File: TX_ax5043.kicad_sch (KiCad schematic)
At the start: 27 parts, among them P6 CONUFL001-SMD-T, P7 CONUFL001-SMD-T, Q7 DMP2037U-7, U23 AX5043

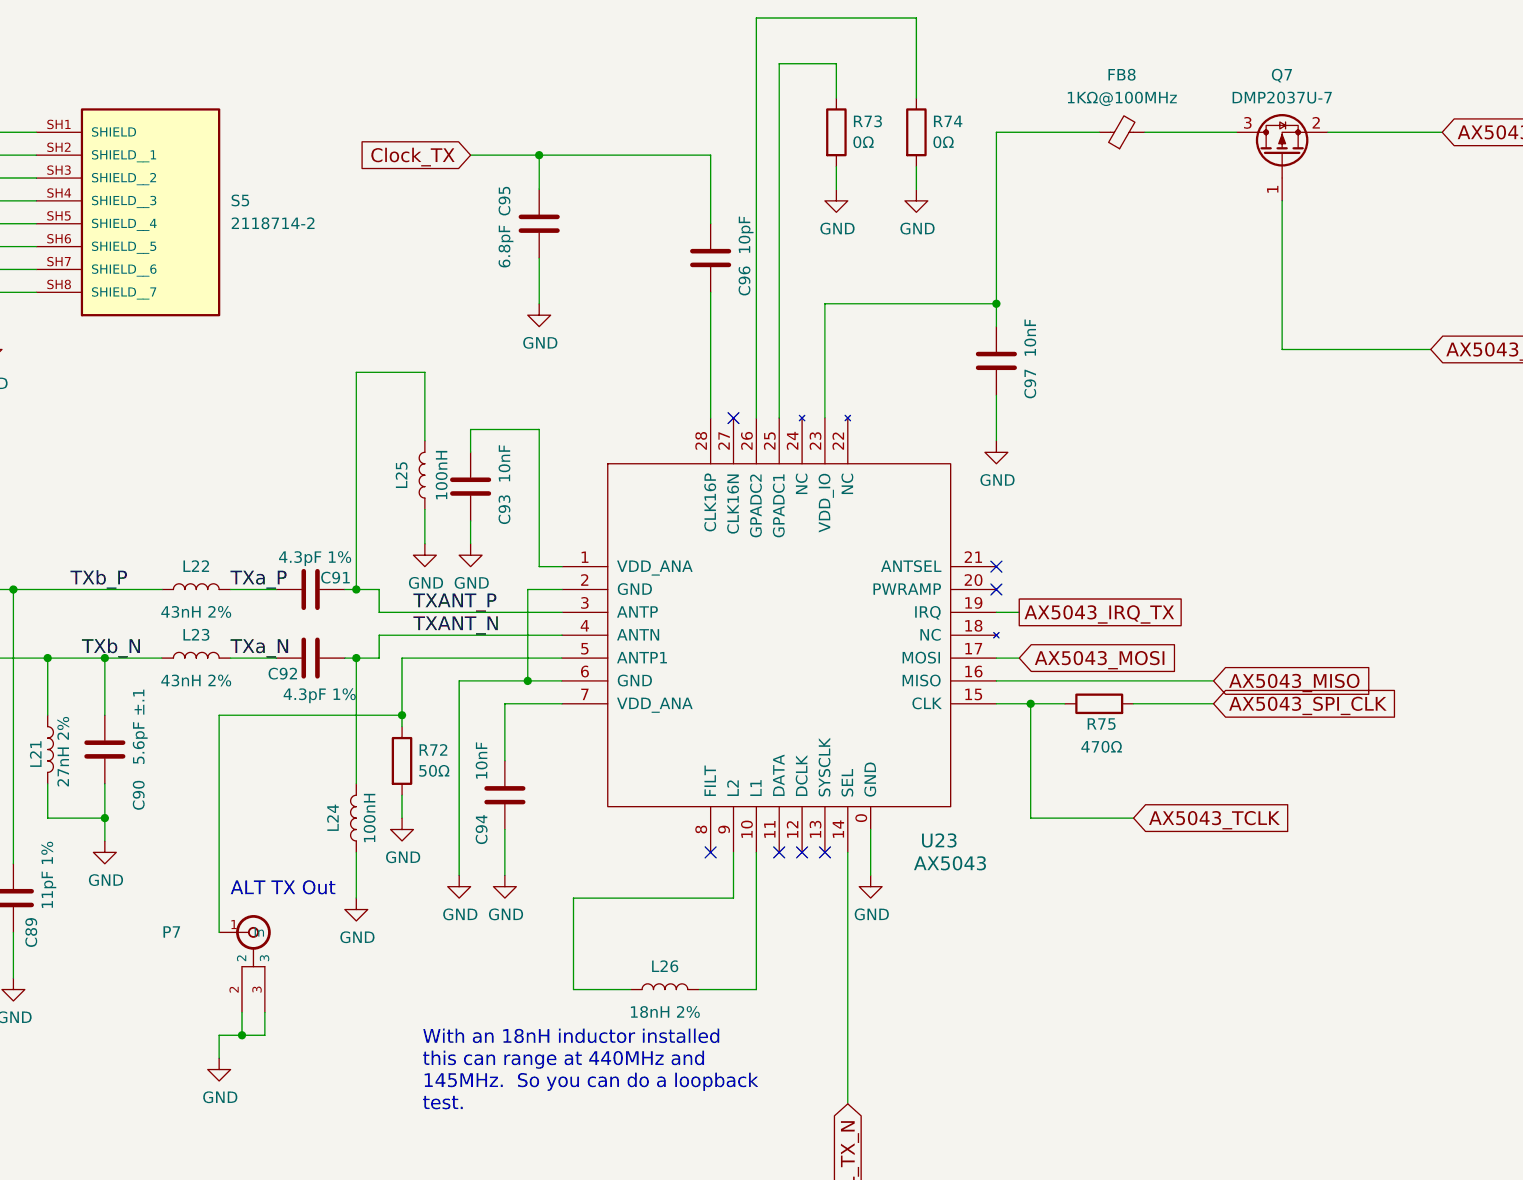
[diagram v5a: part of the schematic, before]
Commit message: Parts replacements for out of stock parts
Signed-off-by: Corey Minyard <corey@minyard.net>
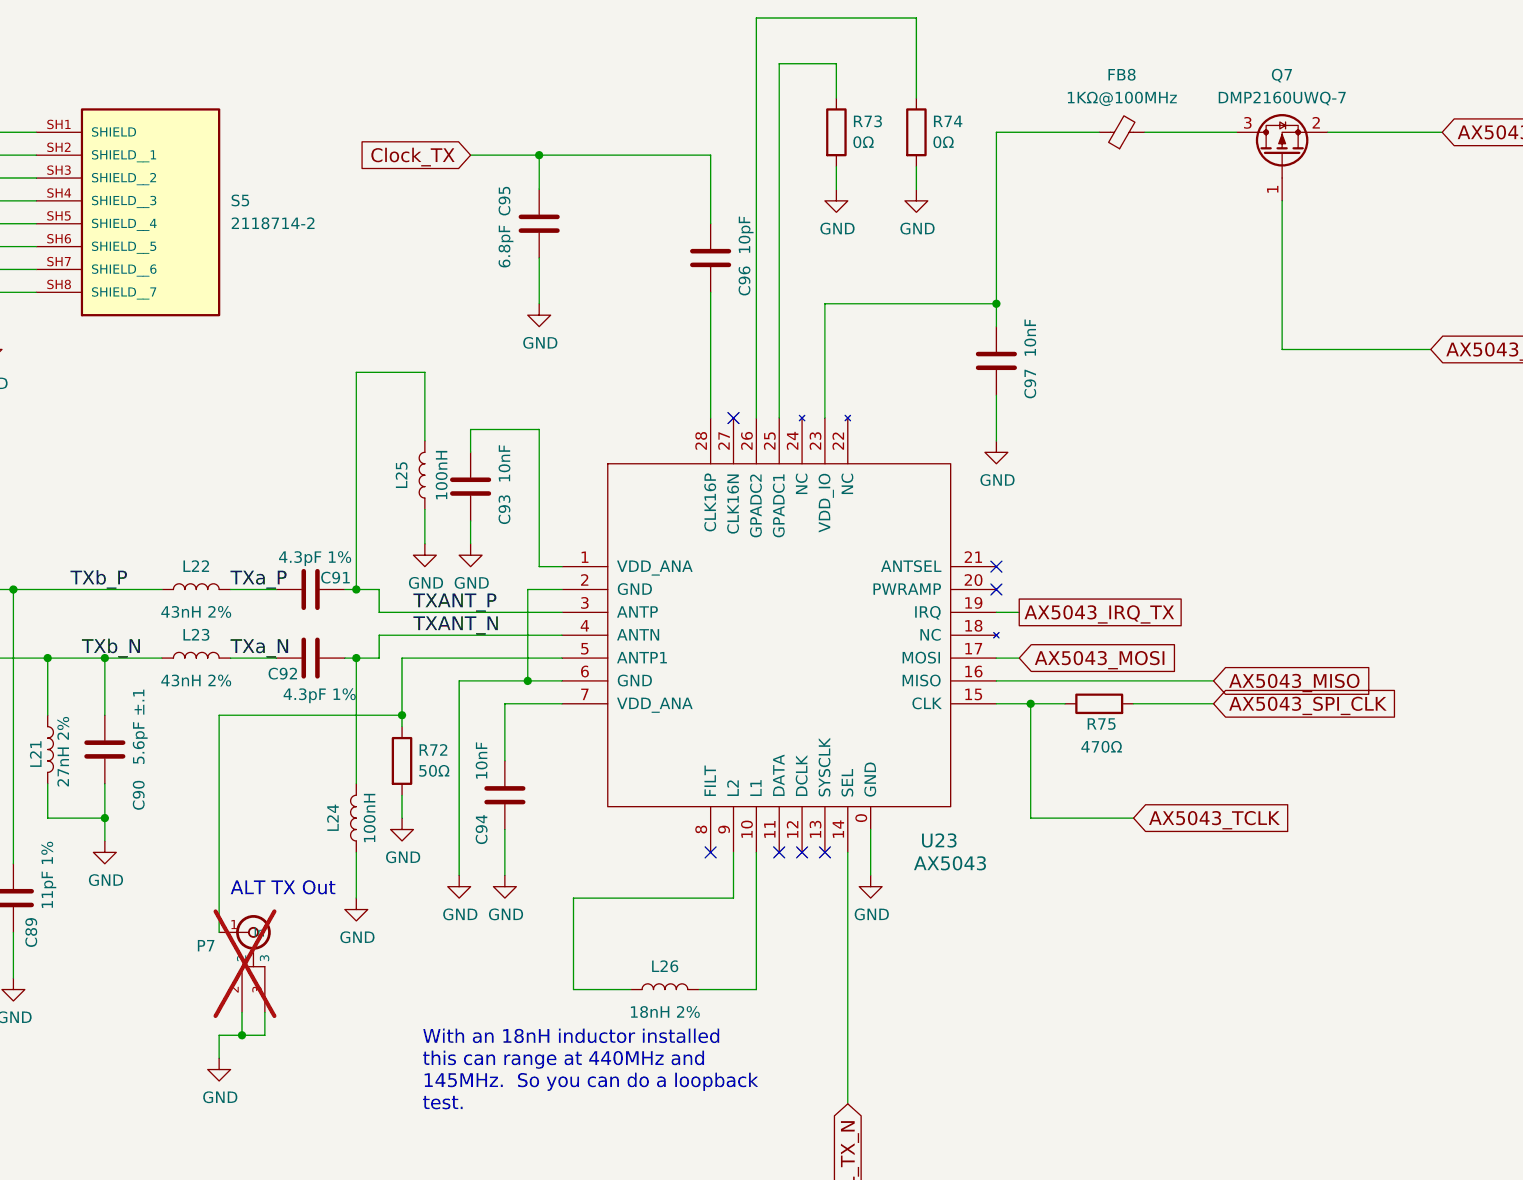
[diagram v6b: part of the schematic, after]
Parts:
- P7: now not fitted; now left out of the parts list
- Q7: value DMP2037U-7 -> DMP2160UWQ-7; footprint Package_TO_SOT_SMD:SOT-23 -> Package_TO_SOT_SMD:SOT-323_SC-70
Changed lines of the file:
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@@
 		(unit 1)
 		(exclude_from_sim no)
-		(in_bom yes)
-		(on_board yes)
-		(dnp no)
+		(in_bom no)
+		(on_board yes)
+		(dnp yes)
 		(property "Reference" "P7"
-			(at 196.85 170.18 0)
+			(at 200.66 171.704 0)
 			(effects
 				(font
@@
 				(path "/cc9f42d2-6985-41ac-acab-5ab7b01c5b38/d9a83ee4-3280-49b9-88b8-54d26cbd8ed1/2fc9a4ba-520e-46cf-be0c-1f13bbb64152"
 					(reference "R75")
+					(unit 1)
+				)
+			)
+		)
+	)
+	(symbol
+		(lib_id "Transistor_FET:Q_PMOS_GSD")
+		(at 321.31 83.82 90)
+		(unit 1)
+		(exclude_from_sim no)
+		(in_bom yes)
+		(on_board yes)
+		(dnp no)
+		(fields_autoplaced yes)
+		(property "Reference" "Q7"
+			(at 321.31 74.93 90)
+			(effects
+				(font
+					(size 1.27 1.27)
+				)
+			)
+		)
+		(property "Value" "DMP2160UWQ-7"
+			(at 321.31 77.47 90)
+			(effects
+				(font
+					(size 1.27 1.27)
+				)
+			)
+		)
+		(property "Footprint" "Package_TO_SOT_SMD:SOT-323_SC-70"
+			(at 318.77 78.74 0)
+			(effects
+				(font
+					(size 1.27 1.27)
+				)
+				(hide yes)
+			)
+		)
+		(property "Datasheet" "~"
+			(at 321.31 83.82 0)
+			(effects
+				(font
+					(size 1.27 1.27)
+				)
+				(hide yes)
+			)
+		)
+		(property "Description" "P-MOSFET transistor, gate/source/drain"
+			(at 321.31 83.82 0)
+			(effects
+				(font
+					(size 1.27 1.27)
+				)
+				(hide yes)
+			)
+		)
+		(pin "2"
+		)
+		(pin "1"
+		)
+		(pin "3"
+		)
+		(instances
+			(project "PacSat_AFSK"
+				(path "/cc9f42d2-6985-41ac-acab-5ab7b01c5b38/d9a83ee4-3280-49b9-88b8-54d26cbd8ed1/2fc9a4ba-520e-46cf-be0c-1f13bbb64152"
+					(reference "Q7")
 					(unit 1)
 				)
@@
 					(unit 1)
 				)
-			)
-		)
-	)
-	(symbol
-		(lib_id "Transistor_FET:Q_PMOS_GSD")
-		(at 321.31 83.82 90)
-		(unit 1)
-		(exclude_from_sim no)
-		(in_bom yes)
-		(on_board yes)
-		(dnp no)
-		(fields_autoplaced yes)
-		(property "Reference" "Q7"
-			(at 321.31 74.93 90)
-			(effects
-				(font
-					(size 1.27 1.27)
-				)
-			)
-		)
-		(property "Value" "DMP2037U-7"
-			(at 321.31 77.47 90)
-			(effects
-				(font
-					(size 1.27 1.27)
-				)
-			)
-		)
-		(property "Footprint" "Package_TO_SOT_SMD:SOT-23"
-			(at 318.77 78.74 0)
-			(effects
-				(font
-					(size 1.27 1.27)
-				)
-				(hide yes)
-			)
-		)
-		(property "Datasheet" "~"
-			(at 321.31 83.82 0)
-			(effects
-				(font
-					(size 1.27 1.27)
-				)
-				(hide yes)
-			)
-		)
-		(property "Description" "P-MOSFET transistor, gate/source/drain"
-			(at 321.31 83.82 0)
-			(effects
-				(font
-					(size 1.27 1.27)
-				)
-				(hide yes)
-			)
-		)
-		(pin "2"
-		)
-		(pin "1"
-		)
-		(pin "3"
-		)
-		(instances
-			(project "PacSat_AFSK"
-				(path "/cc9f42d2-6985-41ac-acab-5ab7b01c5b38/d9a83ee4-3280-49b9-88b8-54d26cbd8ed1/2fc9a4ba-520e-46cf-be0c-1f13bbb64152"
-					(reference "Q7")
-					(unit 1)
-				)
